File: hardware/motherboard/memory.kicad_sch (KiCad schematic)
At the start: 10 parts, among them U3 SN74AHCT164245, U4 SN74AHCT164245

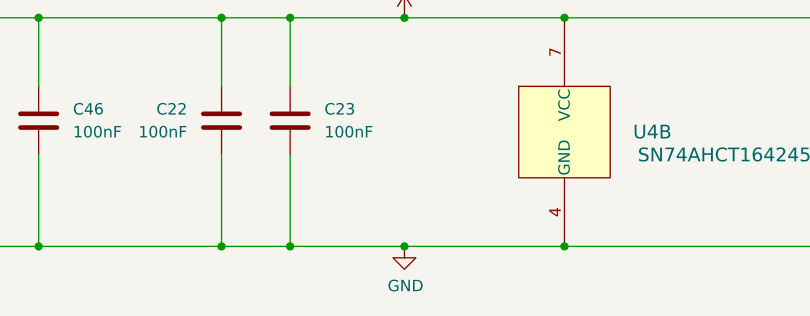
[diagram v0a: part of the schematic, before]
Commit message: restructure, create minimum board project
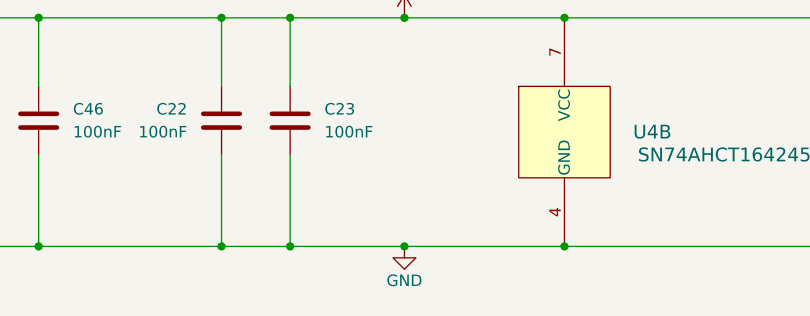
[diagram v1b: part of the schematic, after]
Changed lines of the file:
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@@
     )
   )
-  (symbol (lib_id "UPduino_v3.0:power_GND") (at 81.28 190.5 0) (unit 1)
+  (symbol (lib_id "power:GND") (at 81.28 190.5 0) (unit 1)
     (in_bom yes) (on_board yes) (dnp no)
     (property "Reference" "#PWR042" (at 81.28 196.85 0)
       (effects (font (size 1.27 1.27)) hide)
     )
-    (property "Value" "GND" (at 81.407 194.8942 0)
+    (property "Value" "GND" (at 81.28 194.31 0)
       (effects (font (size 1.27 1.27)))
     )
